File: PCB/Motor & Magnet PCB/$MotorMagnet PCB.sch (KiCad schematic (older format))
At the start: 46 parts, among them K1 CONN_3, K2 CONN_3

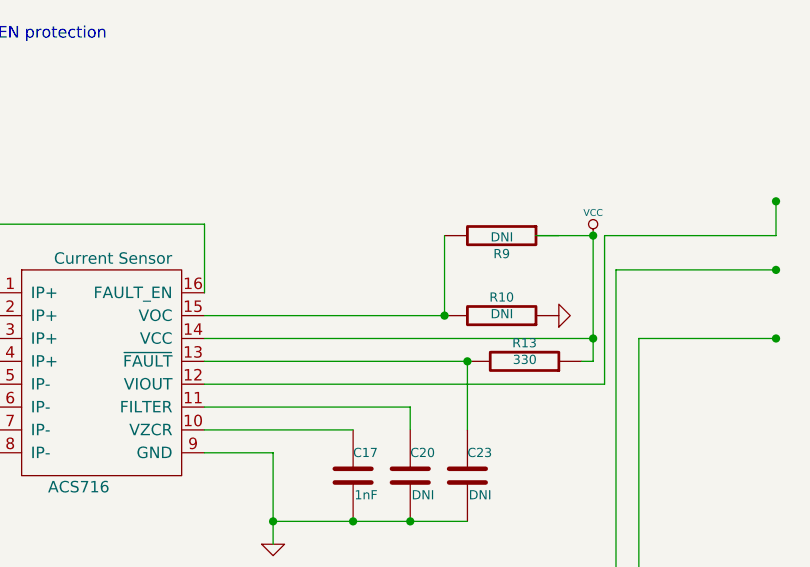
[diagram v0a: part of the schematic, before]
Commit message: Motor/Magnet PCB (KiCad)
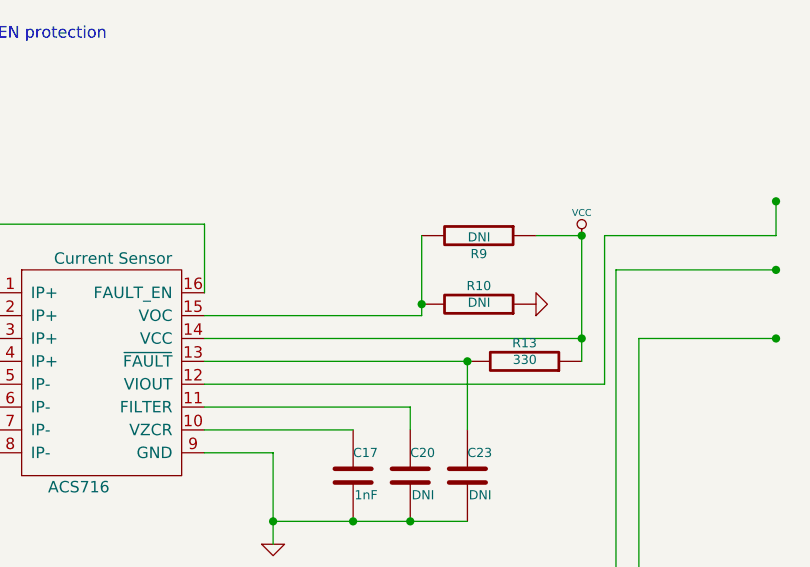
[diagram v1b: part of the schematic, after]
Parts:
- renumbered Current to Current~Sensor, XBEE to XBEE~Chip
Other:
- moved on the sheet: R10, R9
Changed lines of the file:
@@
 PGC
 $Comp
-L ACS716 Current
+L ACS716 Current~Sensor
 U 1 1 51CC9FDA
 P 8150 5050
@@
 $EndComp
 $Comp
-L ACS716 Current
+L ACS716 Current~Sensor
 U 1 1 51CCB665
 P 6950 6700
@@
 $EndComp
 $Comp
-L XBEE-1B2 XBEE
+L XBEE-1B2 XBEE~Chip
 U 1 1 51CCB803
 P 17750 7200
@@
 L VCC #PWR014
 U 1 1 51CDDE39
-P 10400 4450
-F 0 "#PWR014" H 10400 4550 30  0001 C CNN
-F 1 "VCC" H 10400 4550 30  0000 C CNN
-F 2 "" H 10400 4450 60  0000 C CNN
-F 3 "" H 10400 4450 60  0000 C CNN
-	1    10400 4450
+P 10350 4450
+F 0 "#PWR014" H 10350 4550 30  0001 C CNN
+F 1 "VCC" H 10350 4550 30  0000 C CNN
+F 2 "" H 10350 4450 60  0000 C CNN
+F 3 "" H 10350 4450 60  0000 C CNN
+	1    10350 4450
 	1    0    0    -1
 $EndComp
@@
 L R R9
 U 1 1 51CDDE41
-P 10000 4450
-F 0 "R9" V 10080 4450 40  0000 C CNN
-F 1 "DNI" V 10007 4451 40  0000 C CNN
-F 2 "~" V 9930 4450 30  0000 C CNN
-F 3 "~" H 10000 4450 30  0000 C CNN
-	1    10000 4450
+P 9900 4450
+F 0 "R9" V 9980 4450 40  0000 C CNN
+F 1 "DNI" V 9907 4451 40  0000 C CNN
+F 2 "~" V 9830 4450 30  0000 C CNN
+F 3 "~" H 9900 4450 30  0000 C CNN
+	1    9900 4450
 	0    1    1    0
 $EndComp
@@
 L R R10
 U 1 1 51CDDE47
-P 10000 4800
-F 0 "R10" V 10080 4800 40  0000 C CNN
-F 1 "DNI" V 10007 4801 40  0000 C CNN
-F 2 "~" V 9930 4800 30  0000 C CNN
-F 3 "~" H 10000 4800 30  0000 C CNN
-	1    10000 4800
+P 9900 4750
+F 0 "R10" V 9980 4750 40  0000 C CNN
+F 1 "DNI" V 9907 4751 40  0000 C CNN
+F 2 "~" V 9830 4750 30  0000 C CNN
+F 3 "~" H 9900 4750 30  0000 C CNN
+	1    9900 4750
 	0    1    -1   0
 $EndComp
@@
 L GND #PWR015
 U 1 1 51CDDE4D
-P 10250 4800
-F 0 "#PWR015" H 10250 4800 30  0001 C CNN
-F 1 "GND" H 10250 4730 30  0001 C CNN
-F 2 "" H 10250 4800 60  0000 C CNN
-F 3 "" H 10250 4800 60  0000 C CNN
-	1    10250 4800
+P 10150 4750
+F 0 "#PWR015" H 10150 4750 30  0001 C CNN
+F 1 "GND" H 10150 4680 30  0001 C CNN
+F 2 "" H 10150 4750 60  0000 C CNN
+F 3 "" H 10150 4750 60  0000 C CNN
+	1    10150 4750
 	0    -1   -1   0
 $EndComp
@@
 	10500 4600 11200 4600
 Wire Wire Line
-	10400 4450 10400 4900
-Wire Wire Line
-	10400 4900 10400 5000
+	10350 4450 10350 4900
+Wire Wire Line
+	10350 4900 10350 5000
 Wire Wire Line
 	18850 6750 18850 6250
@@
 Connection ~ 9600 5700
 Wire Wire Line
-	10400 5000 10350 5000
-Wire Wire Line
-	10400 4900 8700 4900
-Connection ~ 10400 4900
-Wire Wire Line
-	10400 4450 10150 4450
-Connection ~ 10400 4450
-Wire Wire Line
-	9750 4800 8700 4800
-Wire Wire Line
-	9750 4800 9750 4450
-Connection ~ 9750 4800
+	10350 5000 10350 5000
+Wire Wire Line
+	10350 4900 8700 4900
+Connection ~ 10350 4900
+Wire Wire Line
+	10350 4450 10150 4450
+Connection ~ 10350 4450
+Wire Wire Line
+	9650 4800 8700 4800
+Wire Wire Line
+	9650 4800 9650 4450
 Connection ~ 9850 5000
 Wire Wire Line
@@
 Connection ~ 17600 5650
 Connection ~ 17300 5750
+Connection ~ 9650 4750
 $EndSCHEMATC

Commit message: Motor/Magnet updates
(from earlier in the week)
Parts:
- gave numbers to parts that had none: 13
- renumbered Current to Current1, Current~Sensor to Current2, Current~Sensor to Current3, LED to LED1, R to R16, R to R17, XBEE~Chip to XBEE1
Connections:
- wire segments 210 -> 169
